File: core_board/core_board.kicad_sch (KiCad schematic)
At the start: 58 parts

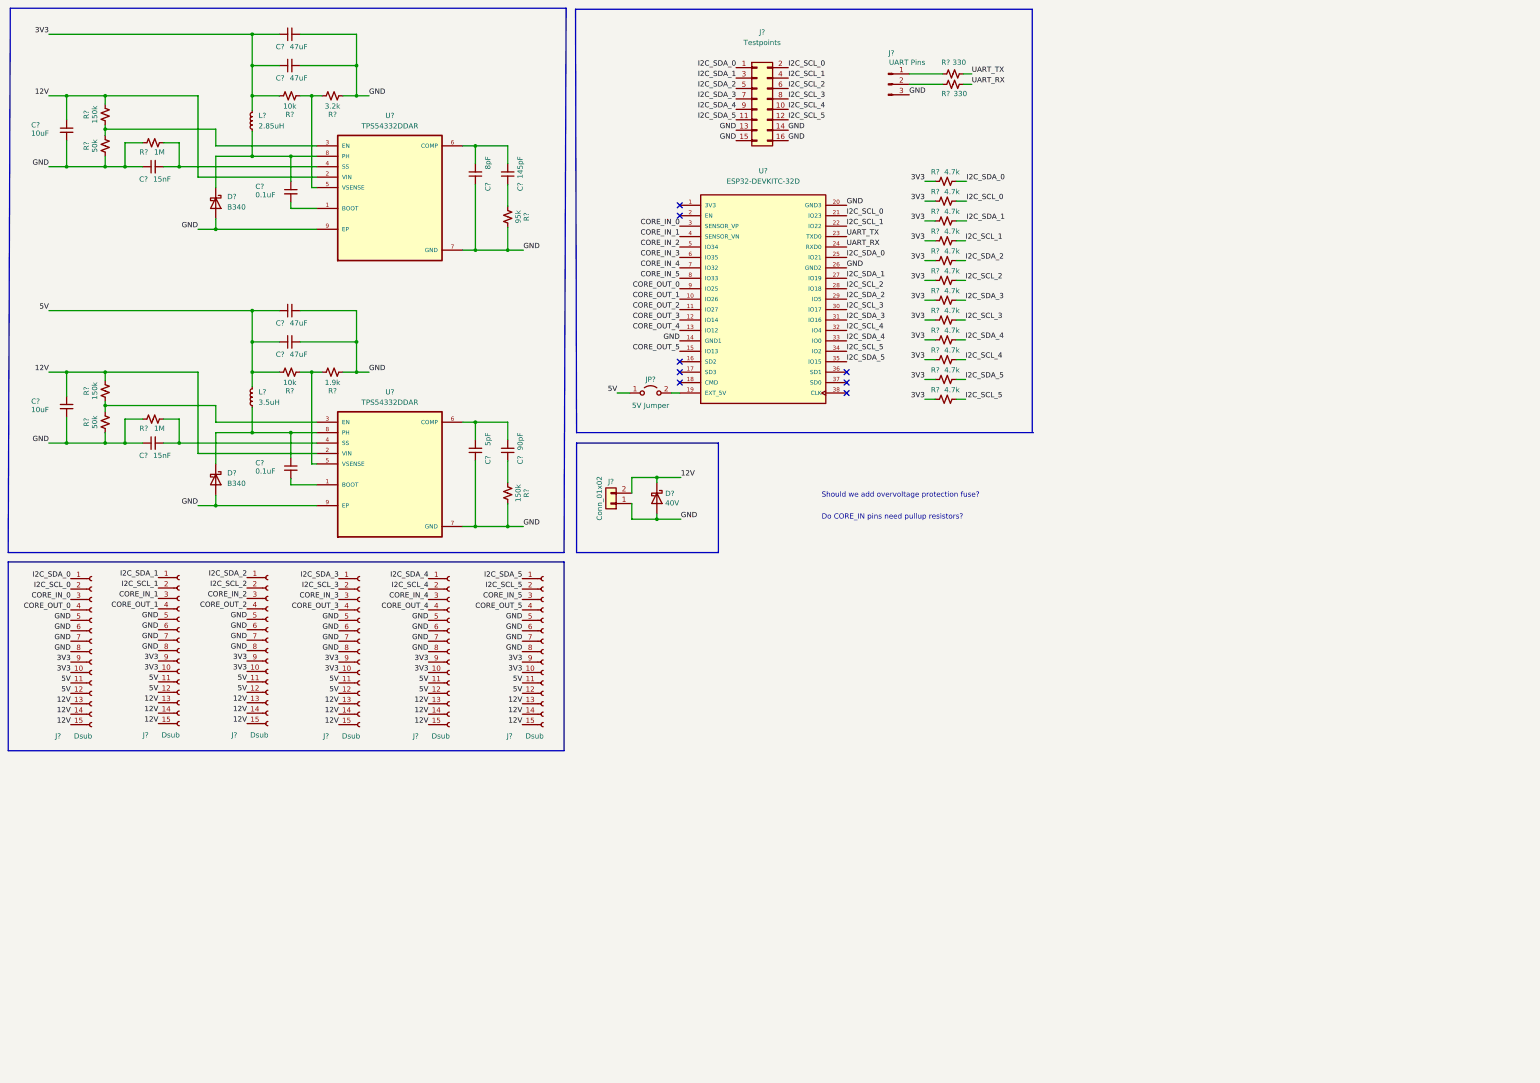
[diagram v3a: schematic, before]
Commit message: Revised schematic based on Trevor's plan
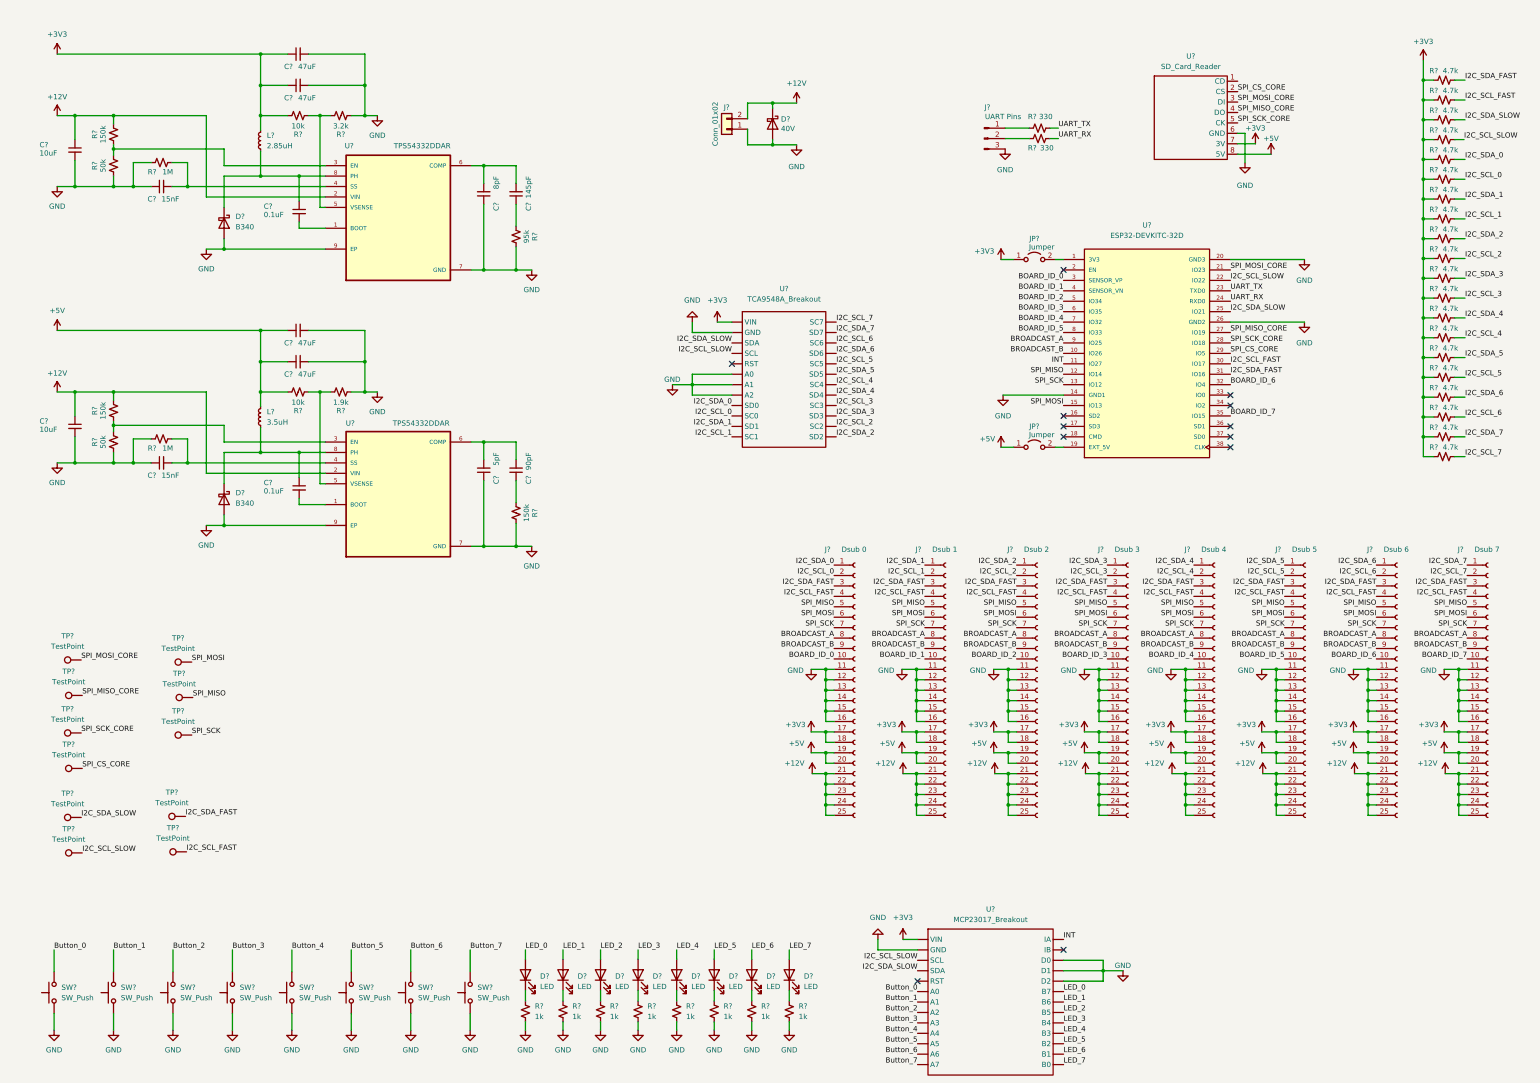
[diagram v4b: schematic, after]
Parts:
- removed J? (x6): Dsub, symbol Connector:Conn_01x15_Female
- removed J?: Testpoints, symbol Connector_Generic:Conn_02x08_Odd_Even
- removed JP?: 5V Jumper, symbol Jumper:Jumper_2_Open
- removed R? (x8): 4.7k, symbol Device:R_Small_US
- added D? (x8): LED, symbol Device:LED
- added J?: Dsub 6, symbol Connector:Conn_01x25_Female
- added J?: Dsub 5, symbol Connector:Conn_01x25_Female
- added J?: Dsub 1, symbol Connector:Conn_01x25_Female
- added J?: Dsub 4, symbol Connector:Conn_01x25_Female
- added J?: Dsub 2, symbol Connector:Conn_01x25_Female
- added J?: Dsub 3, symbol Connector:Conn_01x25_Female
- added J?: Dsub 0, symbol Connector:Conn_01x25_Female
- added J?: Dsub 7, symbol Connector:Conn_01x25_Female
- added JP? (x2): Jumper, symbol Jumper:Jumper_2_Open
- added R? (x16): 4.7k, symbol Device:R_Small_US
- added R? (x8): 1k, symbol Device:R_Small_US
- added SW? (x8): SW_Push, symbol Switch:SW_Push
- added TP? (x11): TestPoint, symbol Connector:TestPoint
- added U?: SD_Card_Reader, symbol ELLIE_Symbol_Library:SD_Card_Reader
- added U?: TCA9548A_Breakout, symbol TCA9548A_Breakout:TCA9548A_Breakout
- added U?: MCP23017_Breakout, symbol MCP23017_Breakout:MCP23017_Breakout
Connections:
- net GND: now also J?.11 (Pin_11), J?.11 (Pin_11), J?.11 (Pin_11), J?.11 (Pin_11), J?.11 (Pin_11), J?.11 (Pin_11), J?.11 (Pin_11), J?.11 (Pin_11), J?.12 (Pin_12), J?.12 (Pin_12), J?.12 (Pin_12), J?.12 (Pin_12), J?.12 (Pin_12), J?.12 (Pin_12), J?.12 (Pin_12), J?.12 (Pin_12), J?.13 (Pin_13), J?.13 (Pin_13), J?.13 (Pin_13), J?.13 (Pin_13), J?.13 (Pin_13), J?.13 (Pin_13), J?.13 (Pin_13), J?.13 (Pin_13), J?.14 (Pin_14), J?.14 (Pin_14), J?.14 (Pin_14), J?.14 (Pin_14), J?.14 (Pin_14), J?.14 (Pin_14), J?.14 (Pin_14), J?.14 (Pin_14), J?.15 (Pin_15), J?.15 (Pin_15), J?.15 (Pin_15), J?.15 (Pin_15), J?.15 (Pin_15), J?.15 (Pin_15), J?.15 (Pin_15), J?.15 (Pin_15), J?.16 (Pin_16), J?.16 (Pin_16), J?.16 (Pin_16), J?.16 (Pin_16), J?.16 (Pin_16), J?.16 (Pin_16), J?.16 (Pin_16), J?.16 (Pin_16), R?.2, R?.2, R?.2, R?.2, R?.2, R?.2, R?.2, R?.2, SW?.1, SW?.1, SW?.1, SW?.1, SW?.1, SW?.1, SW?.1, SW?.1, U?. (VIN), U?. (VIN), U?.6 (GND)
- net I2C_SCL_0: now also J?.2 (Pin_2), R?.2, U?. (VIN); no longer R?.2, U?.21 (IO23)
- net I2C_SCL_1: now also J?.2 (Pin_2), R?.2, U?. (VIN); no longer R?.2, U?.22 (IO22)
- net I2C_SCL_2: now also J?.2 (Pin_2), R?.2, U?. (VIN); no longer U?.28 (IO18)
- net I2C_SCL_3: now also J?.2 (Pin_2), R?.2, U?. (VIN); no longer U?.30 (IO17)
- net I2C_SCL_4: now also J?.2 (Pin_2), R?.2, U?. (VIN); no longer U?.32 (IO4)
- net I2C_SCL_5: now also J?.2 (Pin_2), R?.2, U?. (VIN); no longer U?.34 (IO2)
- net I2C_SDA_0: now also J?.1 (Pin_1), R?.2, U?. (VIN); no longer R?.2, U?.25 (IO21)
- net I2C_SDA_1: now also J?.1 (Pin_1), R?.2, U?. (VIN); no longer R?.2, U?.27 (IO19)
- net I2C_SDA_2: now also J?.1 (Pin_1), R?.2, U?. (VIN); no longer U?.29 (IO5)
- net I2C_SDA_3: now also J?.1 (Pin_1), R?.2, U?. (VIN); no longer U?.31 (IO16)
- net I2C_SDA_4: now also J?.1 (Pin_1), R?.2, U?. (VIN); no longer U?.33 (IO0)
- net I2C_SDA_5: now also J?.1 (Pin_1), R?.2, U?. (VIN); no longer U?.35 (IO15)
- net at U?.19 (EXT_5V): now also JP?.2 (B)
- net at U?.1 (3V3): now also JP?.2 (B)
- net 12V renamed +12V
- net +12V: now also J?.21 (Pin_21), J?.21 (Pin_21), J?.21 (Pin_21), J?.21 (Pin_21), J?.21 (Pin_21), J?.21 (Pin_21), J?.21 (Pin_21), J?.21 (Pin_21), J?.22 (Pin_22), J?.22 (Pin_22), J?.22 (Pin_22), J?.22 (Pin_22), J?.22 (Pin_22), J?.22 (Pin_22), J?.22 (Pin_22), J?.22 (Pin_22), J?.23 (Pin_23), J?.23 (Pin_23), J?.23 (Pin_23), J?.23 (Pin_23), J?.23 (Pin_23), J?.23 (Pin_23), J?.23 (Pin_23), J?.23 (Pin_23), J?.24 (Pin_24), J?.24 (Pin_24), J?.24 (Pin_24), J?.24 (Pin_24), J?.24 (Pin_24), J?.24 (Pin_24), J?.24 (Pin_24), J?.24 (Pin_24), J?.25 (Pin_25), J?.25 (Pin_25), J?.25 (Pin_25), J?.25 (Pin_25), J?.25 (Pin_25), J?.25 (Pin_25), J?.25 (Pin_25), J?.25 (Pin_25)
- net 3V3 renamed +3V3
- net +3V3: now also J?.17 (Pin_17), J?.17 (Pin_17), J?.17 (Pin_17), J?.17 (Pin_17), J?.17 (Pin_17), J?.17 (Pin_17), J?.17 (Pin_17), J?.17 (Pin_17), J?.18 (Pin_18), J?.18 (Pin_18), J?.18 (Pin_18), J?.18 (Pin_18), J?.18 (Pin_18), J?.18 (Pin_18), J?.18 (Pin_18), J?.18 (Pin_18), JP?.1 (A), R?.1, R?.1, R?.1, R?.1, R?.1, R?.1, R?.1, R?.1, R?.1, R?.1, R?.1, R?.1, R?.1, R?.1, R?.1, R?.1, U?. (VIN), U?. (VIN), U?.7 (3V)
- net 5V renamed +5V
- net +5V: now also J?.19 (Pin_19), J?.19 (Pin_19), J?.19 (Pin_19), J?.19 (Pin_19), J?.19 (Pin_19), J?.19 (Pin_19), J?.19 (Pin_19), J?.19 (Pin_19), J?.20 (Pin_20), J?.20 (Pin_20), J?.20 (Pin_20), J?.20 (Pin_20), J?.20 (Pin_20), J?.20 (Pin_20), J?.20 (Pin_20), J?.20 (Pin_20), JP?.1 (A), U?.8 (5V)
- net CORE_IN_0 renamed BOARD_ID_0
- net BOARD_ID_0: now also J?.10 (Pin_10)
- net CORE_IN_1 renamed BOARD_ID_1
- net BOARD_ID_1: now also J?.10 (Pin_10)
- net CORE_IN_2 renamed BOARD_ID_2
- net BOARD_ID_2: now also J?.10 (Pin_10)
- net CORE_IN_3 renamed BOARD_ID_3
- net BOARD_ID_3: now also J?.10 (Pin_10)
- net CORE_IN_4 renamed BOARD_ID_4
- net BOARD_ID_4: now also J?.10 (Pin_10)
- net CORE_IN_5 renamed BOARD_ID_5
- net BOARD_ID_5: now also J?.10 (Pin_10)
- net CORE_OUT_0 renamed BROADCAST_A
- net BROADCAST_A: now also J?.8 (Pin_8), J?.8 (Pin_8), J?.8 (Pin_8), J?.8 (Pin_8), J?.8 (Pin_8), J?.8 (Pin_8), J?.8 (Pin_8), J?.8 (Pin_8)
- net CORE_OUT_1 renamed BROADCAST_B
- net BROADCAST_B: now also J?.9 (Pin_9), J?.9 (Pin_9), J?.9 (Pin_9), J?.9 (Pin_9), J?.9 (Pin_9), J?.9 (Pin_9), J?.9 (Pin_9), J?.9 (Pin_9)
- net CORE_OUT_2 renamed INT
- net INT: now also U?. (VIN)
- net CORE_OUT_3 renamed SPI_MISO
- net SPI_MISO: now also J?.5 (Pin_5), J?.5 (Pin_5), J?.5 (Pin_5), J?.5 (Pin_5), J?.5 (Pin_5), J?.5 (Pin_5), J?.5 (Pin_5), J?.5 (Pin_5), TP?.1
- net CORE_OUT_4 renamed SPI_SCK
- net SPI_SCK: now also J?.7 (Pin_7), J?.7 (Pin_7), J?.7 (Pin_7), J?.7 (Pin_7), J?.7 (Pin_7), J?.7 (Pin_7), J?.7 (Pin_7), J?.7 (Pin_7), TP?.1
- net CORE_OUT_5 renamed SPI_MOSI
- net SPI_MOSI: now also J?.6 (Pin_6), J?.6 (Pin_6), J?.6 (Pin_6), J?.6 (Pin_6), J?.6 (Pin_6), J?.6 (Pin_6), J?.6 (Pin_6), J?.6 (Pin_6), TP?.1
- new net: D?.1 (K), R?.1 (x8)
- new net BOARD_ID_6: J?.10 (Pin_10), U?.32 (IO4)
- new net BOARD_ID_7: J?.10 (Pin_10), U?.35 (IO15)
- new net Button_0: SW?.2, U?. (VIN)
- new net Button_1: SW?.2, U?. (VIN)
- new net Button_2: SW?.2, U?. (VIN)
- new net Button_3: SW?.2, U?. (VIN)
- new net Button_4: SW?.2, U?. (VIN)
- new net Button_5: SW?.2, U?. (VIN)
- new net Button_6: SW?.2, U?. (VIN)
- new net Button_7: SW?.2, U?. (VIN)
- new net I2C_SCL_6: J?.2 (Pin_2), R?.2, U?. (VIN)
- new net I2C_SCL_7: J?.2 (Pin_2), R?.2, U?. (VIN)
- new net I2C_SCL_FAST: J?.4 (Pin_4), J?.4 (Pin_4), J?.4 (Pin_4), J?.4 (Pin_4), J?.4 (Pin_4), J?.4 (Pin_4), J?.4 (Pin_4), J?.4 (Pin_4), R?.2, TP?.1, U?.30 (IO17)
- new net I2C_SCL_SLOW: R?.2, TP?.1, U?. (VIN), U?. (VIN), U?.22 (IO22)
- new net I2C_SDA_6: J?.1 (Pin_1), R?.2, U?. (VIN)
- new net I2C_SDA_7: J?.1 (Pin_1), R?.2, U?. (VIN)
- new net I2C_SDA_FAST: J?.3 (Pin_3), J?.3 (Pin_3), J?.3 (Pin_3), J?.3 (Pin_3), J?.3 (Pin_3), J?.3 (Pin_3), J?.3 (Pin_3), J?.3 (Pin_3), R?.2, TP?.1, U?.31 (IO16)
- new net I2C_SDA_SLOW: R?.2, TP?.1, U?. (VIN), U?. (VIN), U?.25 (IO21)
- new net LED_0: D?.2 (A), U?. (VIN)
- new net LED_1: D?.2 (A), U?. (VIN)
- new net LED_2: D?.2 (A), U?. (VIN)
- new net LED_3: D?.2 (A), U?. (VIN)
- new net LED_4: D?.2 (A), U?. (VIN)
- new net LED_5: D?.2 (A), U?. (VIN)
- new net LED_6: D?.2 (A), U?. (VIN)
- new net LED_7: D?.2 (A), U?. (VIN)
- new net SPI_CS_CORE: TP?.1, U?.2 (CS), U?.29 (IO5)
- new net SPI_MISO_CORE: TP?.1, U?.27 (IO19), U?.4 (DO)
- new net SPI_MOSI_CORE: TP?.1, U?.21 (IO23), U?.3 (DI)
- new net SPI_SCK_CORE: TP?.1, U?.28 (IO18), U?.5 (CK)
- no-connect marks 8 -> 12
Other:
- note removed: "Do CORE_IN pins need pullup resistors?"
- note removed: "Should we add overvoltage protection fuse?"
- moved on the sheet: C?, D?, J?, L?, R?, U?

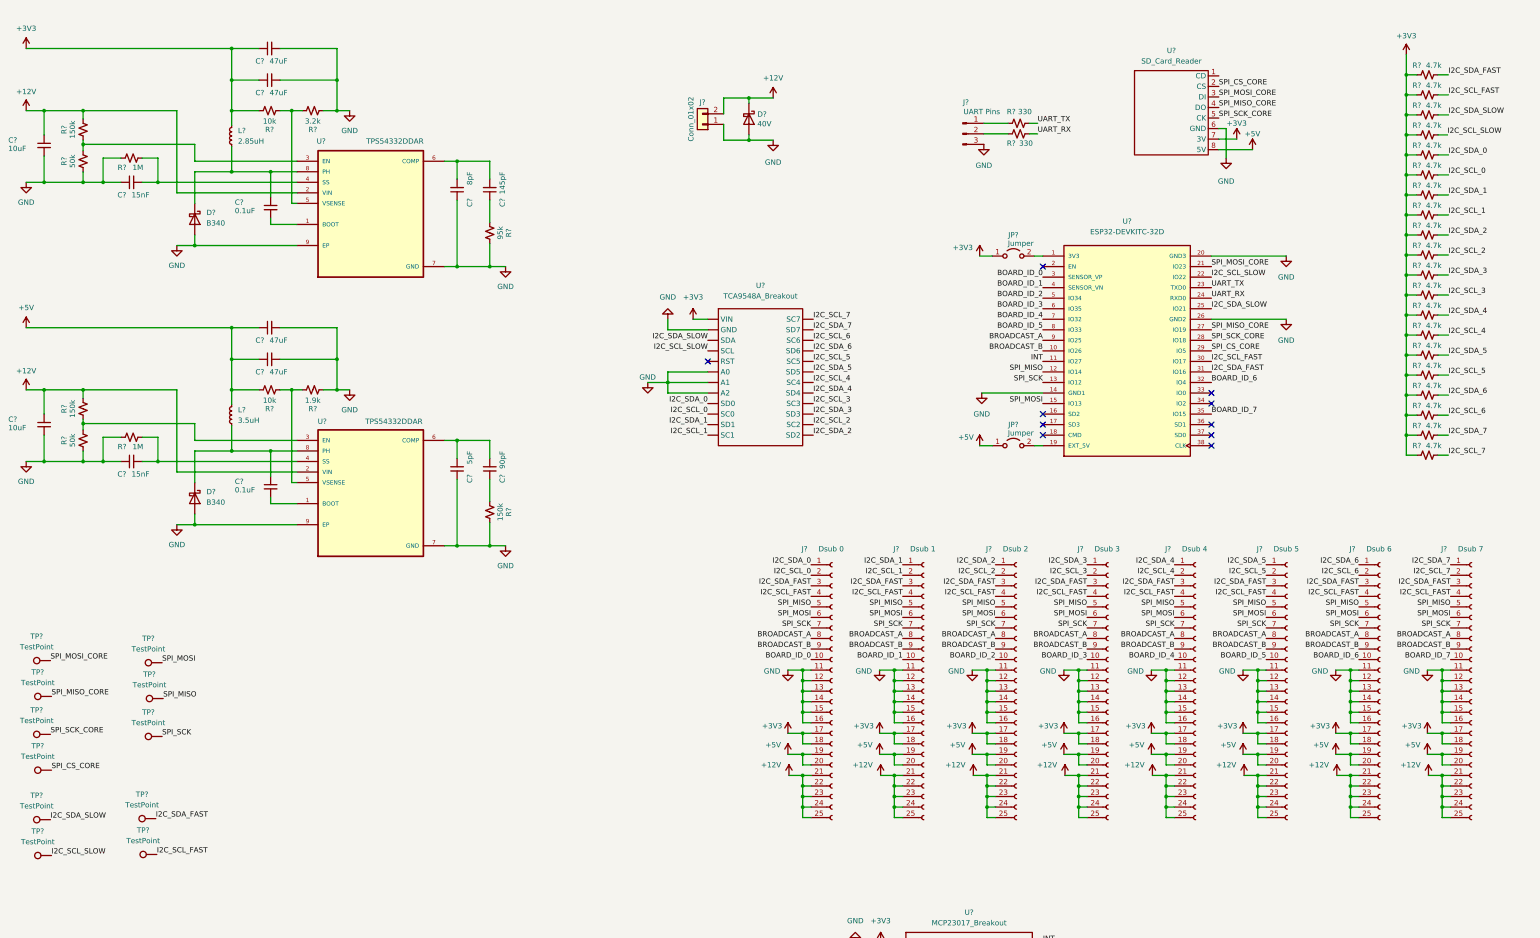
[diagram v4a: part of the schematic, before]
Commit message: incorporated changed from design review meeting
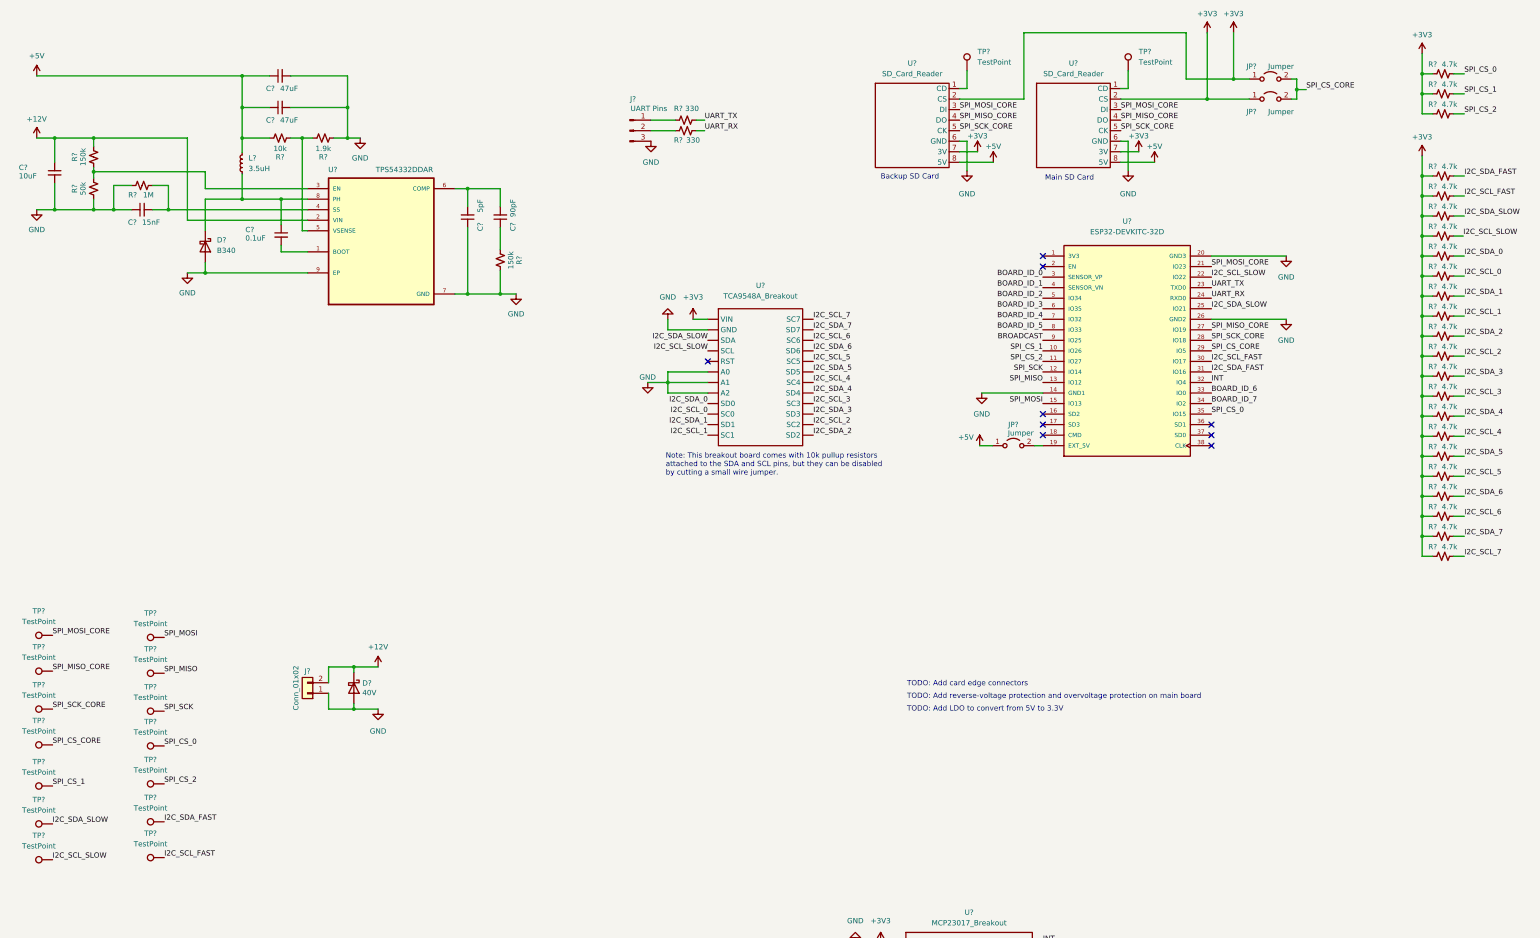
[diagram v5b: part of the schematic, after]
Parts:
- removed C?: 10uF, symbol Device:C_Small
- removed C? (x2): 47uF, symbol Device:C_Small
- removed C?: 145pF, symbol Device:C_Small
- removed C?: 8pF, symbol Device:C_Small
- removed C?: 15nF, symbol Device:C_Small
- removed C?: 0.1uF, symbol Device:C_Small
- removed D?: B340, Diode_SMD:D_SMC, symbol Diode:B340
- removed J?: Dsub 6, symbol Connector:Conn_01x25_Female
- removed J?: Dsub 5, symbol Connector:Conn_01x25_Female
- removed J?: Dsub 1, symbol Connector:Conn_01x25_Female
- removed J?: Dsub 4, symbol Connector:Conn_01x25_Female
- removed J?: Dsub 2, symbol Connector:Conn_01x25_Female
- removed J?: Dsub 3, symbol Connector:Conn_01x25_Female
- removed J?: Dsub 0, symbol Connector:Conn_01x25_Female
- removed J?: Dsub 7, symbol Connector:Conn_01x25_Female
- removed JP?: Jumper, symbol Jumper:Jumper_2_Open
- removed L?: 2.85uH, symbol Device:L_Small
- removed R?: 150k, symbol Device:R_Small_US
- removed R?: 10k, symbol Device:R_Small_US
- removed R?: 3.2k, symbol Device:R_Small_US
- removed R?: 1M, symbol Device:R_Small_US
- removed R?: 95k, symbol Device:R_Small_US
- removed R?: 50k, symbol Device:R_Small_US
- removed U?: TPS54332DDAR, VREG_LM5017MR/NOPB, symbol TPS54332DDAR:TPS54332DDAR
- added JP? (x2): Jumper, symbol Jumper:Jumper_2_Open
- added R? (x3): 4.7k, symbol Device:R_Small_US
- added TP? (x5): TestPoint, symbol Connector:TestPoint
- added U?: SD_Card_Reader, symbol ELLIE_Symbol_Library:SD_Card_Reader
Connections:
- net +3V3: now also U?.2 (CS), JP?.1 (A), JP?.1 (A), R?.1, R?.1, R?.1, U?.2 (CS), U?.7 (3V)
- net +5V: now also U?.8 (5V)
- net BOARD_ID_6: now also U?.33 (IO0); no longer U?.32 (IO4)
- net BOARD_ID_7: now also U?.34 (IO2); no longer U?.35 (IO15)
- net GND: now also U?.6 (GND)
- net INT: now also U?.32 (IO4); no longer U?.11 (IO27)
- net SPI_CS_CORE: now also JP?.2 (B), JP?.2 (B); no longer U?.2 (CS)
- net SPI_MISO: now also U?.13 (IO12); no longer U?.12 (IO14)
- net SPI_MISO_CORE: now also U?.4 (DO)
- net SPI_MOSI_CORE: now also U?.3 (DI)
- net SPI_SCK: now also U?.12 (IO14); no longer U?.13 (IO12)
- net SPI_SCK_CORE: now also U?.5 (CK)
- net at U?.1 (CD): now also TP?.1
- net BROADCAST_A renamed BROADCAST
- net BROADCAST_B renamed SPI_CS_1
- net SPI_CS_1: now also R?.2, TP?.1
- new net: TP?.1, U?.1 (CD)
- new net SPI_CS_0: R?.2, TP?.1, U?.35 (IO15)
- new net SPI_CS_2: R?.2, TP?.1, U?.11 (IO27)
- no-connect marks 12 -> 11
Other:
- note added: "Backup SD Card"
- note added: "Main SD Card"
- note added: "Note: This breakout board comes with 10k pullup resistors attached to the SDA and SCL pins, but they can be disabled by cutting a small wire jumper."
- note added: "TODO: Add LDO to convert from 5V to 3.3V"
- note added: "TODO: Add card edge connectors"
- note added: "TODO: Add reverse-voltage protection and overvoltage protection on main board"
- moved on the sheet: C?, D?, J?, L?, R?, TP?, U?
